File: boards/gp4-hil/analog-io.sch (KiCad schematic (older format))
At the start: 147 parts, among them U10 AD9609, U11 DAC084S085, U12 DAC084S085, U13 DAC084S085, U14 DAC084S085, U19 TS3A4751, U2 XC7A100T-1FTG256C, U25 TS3A4751, U26 TS3A4751, U27 TS3A4751, U28 TS3A4751, U31 ADA4937-2, U8 ADG726, U9 AD9609

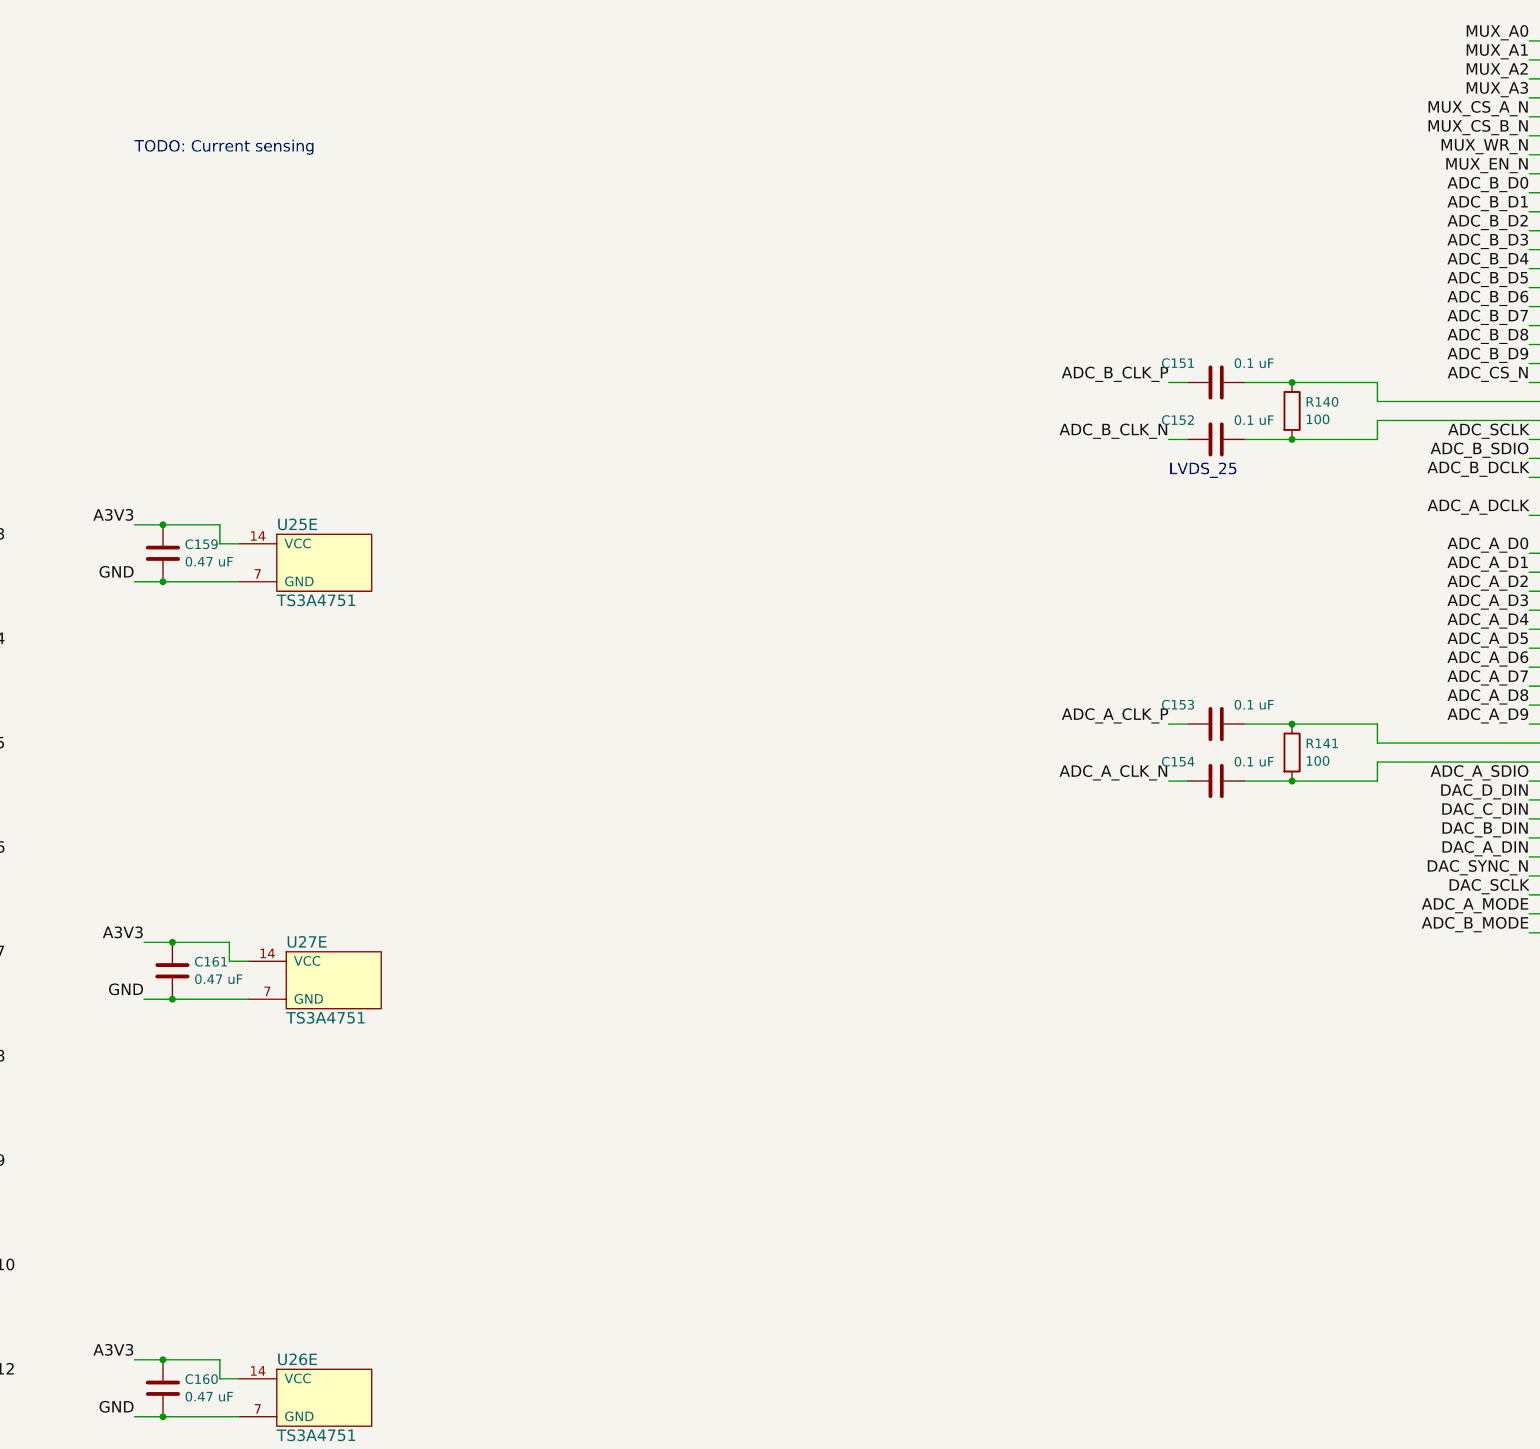
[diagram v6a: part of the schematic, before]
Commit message: Added current monitoring shunts. Began design review
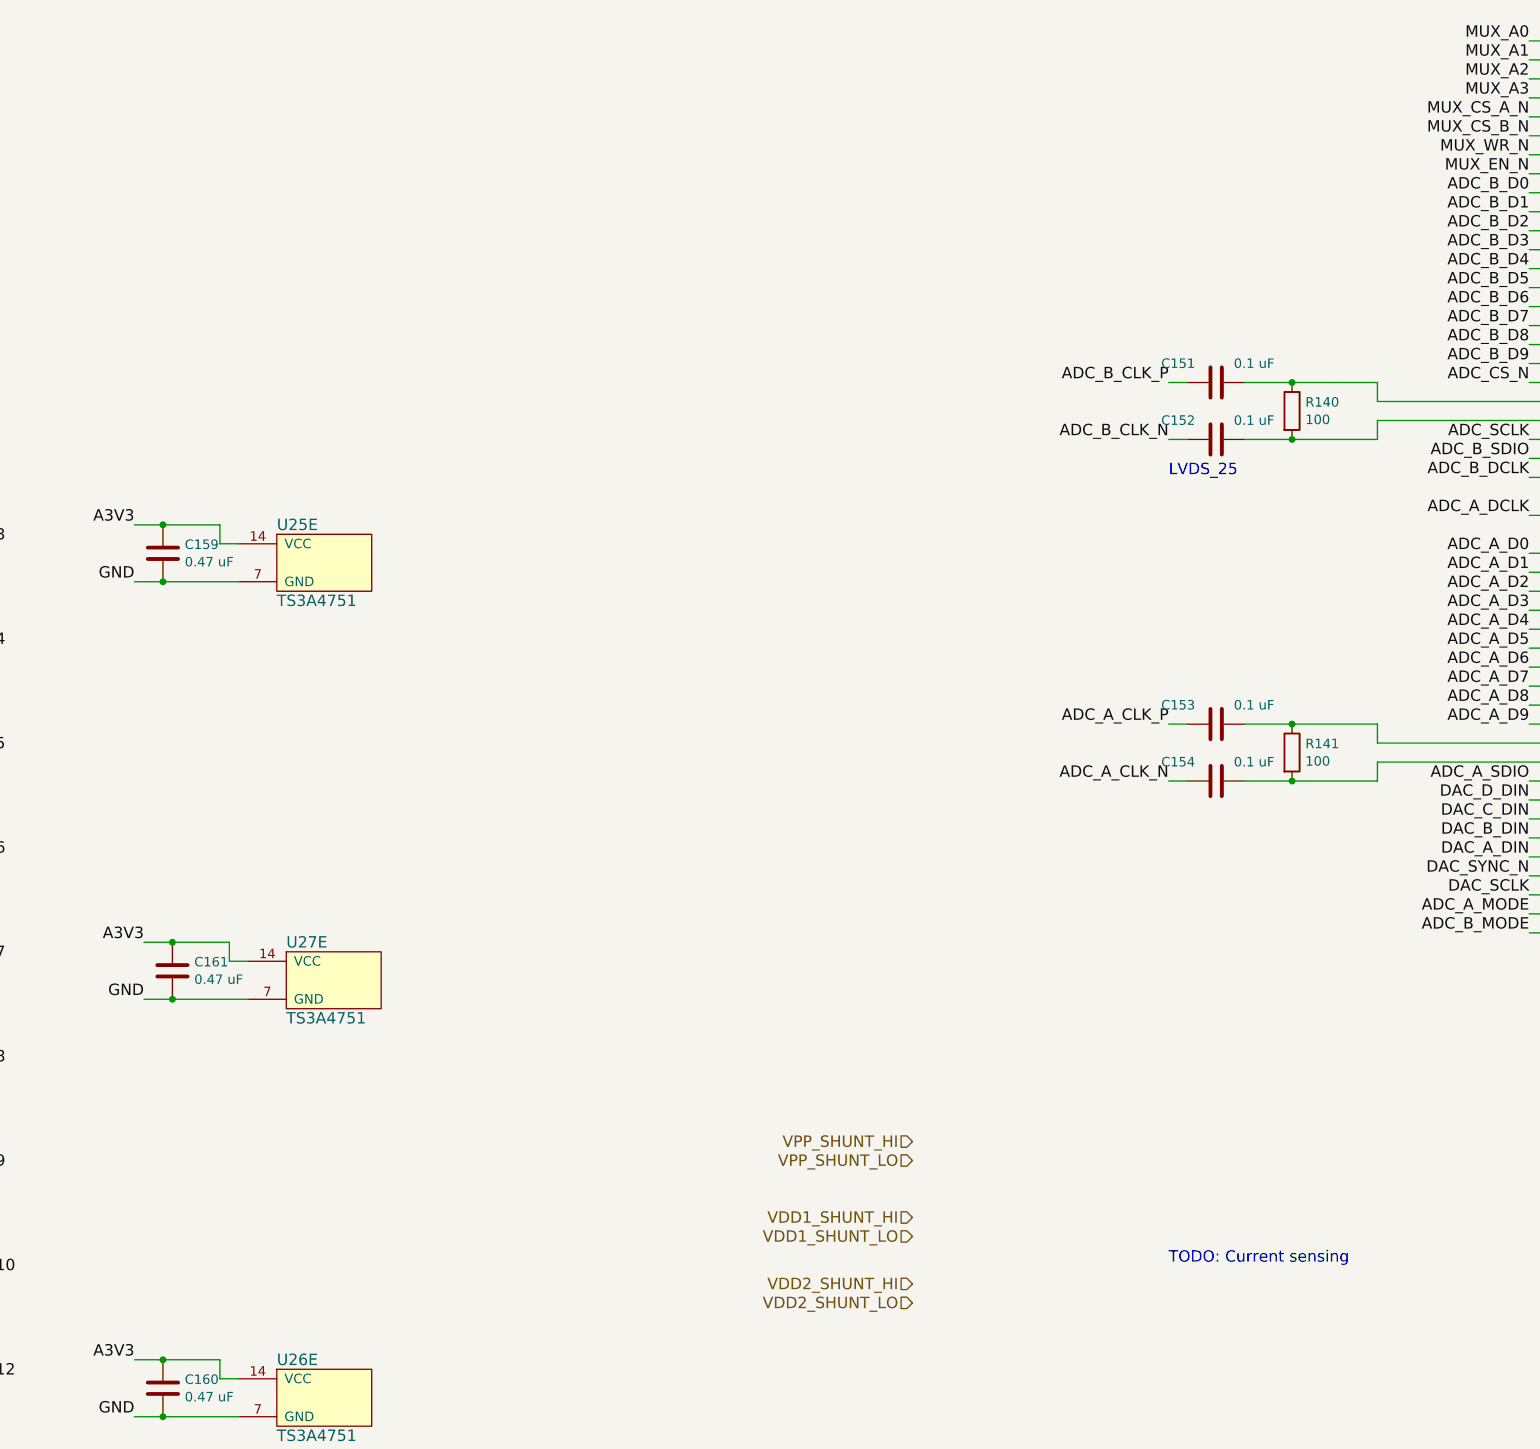
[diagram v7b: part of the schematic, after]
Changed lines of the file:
@@
 Sheet 5 7
 Title "GreenPak Hardware-In-Loop Test Platform"
-Date "2016-05-17"
+Date "2016-05-18"
 Rev "0.1"
 Comp "Andrew Zonenberg"
@@
 Text Label 20550 1850 2    60   ~ 0
 MUX_EN_N
-Text Notes 13200 1750 0    60   ~ 0
+Text Notes 18650 7600 0    60   ~ 0
 TODO: Current sensing
 $Comp
@@
 Wire Wire Line
 	1300 700  1500 700
+Text HLabel 17300 6950 0    60   Input ~ 0
+VPP_SHUNT_HI
+Text HLabel 17300 7050 0    60   Input ~ 0
+VPP_SHUNT_LO
+Text HLabel 17300 7350 0    60   Input ~ 0
+VDD1_SHUNT_HI
+Text HLabel 17300 7450 0    60   Input ~ 0
+VDD1_SHUNT_LO
+Text HLabel 17300 7700 0    60   Input ~ 0
+VDD2_SHUNT_HI
+Text HLabel 17300 7800 0    60   Input ~ 0
+VDD2_SHUNT_LO
 $EndSCHEMATC

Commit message: Added shunt amplifiers and connected to ADC
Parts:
- added C176, C177, C178: 0.1 uF, symbol C
- added U34, U35, U36: INA199A2RSW, symbol INA199AX-RSW
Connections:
- net A3V3: now also C176.1, C177.1, C178.1, U34.6 (VDD), U35.6 (VDD), U36.6 (VDD)
- net GND: now also C176.2, C177.2, C178.2, U34.8 (REF), U34.9 (GND), U35.8 (REF), U35.9 (GND), U36.8 (REF), U36.9 (GND)
- net VDD1_SHUNT_HI: now also U35.2 (IN+), U35.3 (IN+)
- net VDD1_SHUNT_LO: now also U35.4 (IN-), U35.5 (IN-)
- net VDD2_SHUNT_HI: now also U36.2 (IN+), U36.3 (IN+)
- net VDD2_SHUNT_LO: now also U36.4 (IN-), U36.5 (IN-)
- net VPP_SHUNT_HI: now also U34.2 (IN+), U34.3 (IN+)
- net VPP_SHUNT_LO: now also U34.4 (IN-), U34.5 (IN-)
- net VDD2_ISENSE: now reaches U8.36 (S12B)
- net VDD2_ISENSE: now also U36.10 (OUT)
- net VDD1_ISENSE: now reaches U8.4 (S13A)
- net VDD1_ISENSE: now also U35.10 (OUT)
- net VPP_ISENSE: now reaches U8.5 (S12A)
- net VPP_ISENSE: now also U34.10 (OUT)
- no-connect marks 17 -> 14
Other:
- note added: "DUT current metering"
- note removed: "TODO: Current sensing"
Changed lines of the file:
@@
 Sheet 5 7
 Title "GreenPak Hardware-In-Loop Test Platform"
-Date "2016-05-18"
+Date "2016-05-19"
 Rev "0.1"
 Comp "Andrew Zonenberg"
-Comment1 ""
+Comment1 "ADCs and DACs"
 Comment2 ""
 Comment3 ""
@@
 	1    0    0    -1
 $EndComp
-NoConn ~ 1650 6350
-NoConn ~ 1650 6450
 NoConn ~ 1650 6550
 NoConn ~ 1650 6650
 NoConn ~ 1650 6750
-NoConn ~ 3050 6350
 NoConn ~ 3050 6450
 NoConn ~ 3050 6550
@@
 Text Label 20550 1850 2    60   ~ 0
 MUX_EN_N
-Text Notes 18650 7600 0    60   ~ 0
-TODO: Current sensing
+Text Notes 17150 12250 0    60   ~ 0
+DUT current metering
 $Comp
 L AD9609 U9
@@
 	3050 6050 3150 6050
 Wire Wire Line
-	3150 6250 3050 6250
+	3050 6250 3450 6250
 Wire Wire Line
 	1700 7550 2950 7550
@@
 NoConn ~ 7650 7800
 NoConn ~ 7650 7600
-Text HLabel 3150 6250 2    60   Input ~ 0
+Text HLabel 3450 6250 2    60   Input ~ 0
 PSU_VTEMP
 Wire Wire Line
@@
 Wire Wire Line
 	1300 700  1500 700
-Text HLabel 17300 6950 0    60   Input ~ 0
+Text HLabel 17300 9350 0    60   Input ~ 0
 VPP_SHUNT_HI
-Text HLabel 17300 7050 0    60   Input ~ 0
+Text HLabel 17300 9450 0    60   Input ~ 0
 VPP_SHUNT_LO
-Text HLabel 17300 7350 0    60   Input ~ 0
+Text HLabel 17300 10550 0    60   Input ~ 0
 VDD1_SHUNT_HI
-Text HLabel 17300 7450 0    60   Input ~ 0
+Text HLabel 17300 10650 0    60   Input ~ 0
 VDD1_SHUNT_LO
-Text HLabel 17300 7700 0    60   Input ~ 0
+Text HLabel 17300 11700 0    60   Input ~ 0
 VDD2_SHUNT_HI
-Text HLabel 17300 7800 0    60   Input ~ 0
+Text HLabel 17300 11800 0    60   Input ~ 0
 VDD2_SHUNT_LO
+$Comp
+L INA199AX-RSW U34
+U 1 1 576C8568
+P 17750 9600
+F 0 "U34" H 17750 9550 60  0000 L CNN
+F 1 "INA199A2RSW" H 18550 9550 60  0000 R CNN
+F 2 "" H 17750 9600 60  0000 C CNN
+F 3 "" H 17750 9600 60  0000 C CNN
+	1    17750 9600
+	1    0    0    -1
+$EndComp
+Text Label 16750 8750 2    60   ~ 0
+A3V3
+Text Label 16750 9050 2    60   ~ 0
+GND
+Wire Wire Line
+	17300 9350 17450 9350
+Wire Wire Line
+	17450 9250 17350 9250
+Wire Wire Line
+	17350 9250 17350 9350
+Connection ~ 17350 9350
+Wire Wire Line
+	17300 9450 17450 9450
+Wire Wire Line
+	17450 9550 17350 9550
+Wire Wire Line
+	17350 9550 17350 9450
+Connection ~ 17350 9450
+Wire Wire Line
+	16750 9050 17450 9050
+$Comp
+L C C176
+U 1 1 576CB8B1
+P 16900 8900
+F 0 "C176" H 17015 8946 50  0000 L CNN
+F 1 "0.1 uF" H 17015 8854 50  0000 L CNN
+F 2 "" H 16938 8750 30  0000 C CNN
+F 3 "" H 16900 8900 60  0000 C CNN
+	1    16900 8900
+	1    0    0    -1
+$EndComp
+Connection ~ 16900 9050
+Wire Wire Line
+	16750 8750 17450 8750
+Connection ~ 16900 8750
+Wire Wire Line
+	17450 8750 17450 8850
+Wire Wire Line
+	17450 8950 17350 8950
+Wire Wire Line
+	17350 8950 17350 9050
+Connection ~ 17350 9050
+Text Label 19000 9400 0    60   ~ 0
+VPP_ISENSE
+Wire Wire Line
+	19000 9400 18800 9400
+$Comp
+L INA199AX-RSW U35
+U 1 1 576D207C
+P 17750 10800
+F 0 "U35" H 17750 10750 60  0000 L CNN
+F 1 "INA199A2RSW" H 18550 10750 60  0000 R CNN
+F 2 "" H 17750 10800 60  0000 C CNN
+F 3 "" H 17750 10800 60  0000 C CNN
+	1    17750 10800
+	1    0    0    -1
+$EndComp
+Text Label 16750 9950 2    60   ~ 0
+A3V3
+Text Label 16750 10250 2    60   ~ 0
+GND
+Wire Wire Line
+	17300 10550 17450 10550
+Wire Wire Line
+	17450 10450 17350 10450
+Wire Wire Line
+	17350 10450 17350 10550
+Connection ~ 17350 10550
+Wire Wire Line
+	17300 10650 17450 10650
+Wire Wire Line
+	17450 10750 17350 10750
+Wire Wire Line
+	17350 10750 17350 10650
+Connection ~ 17350 10650
+Wire Wire Line
+	16750 10250 17450 10250
+$Comp
+L C C177
+U 1 1 576D208D
+P 16900 10100
+F 0 "C177" H 17015 10146 50  0000 L CNN
+F 1 "0.1 uF" H 17015 10054 50  0000 L CNN
+F 2 "" H 16938 9950 30  0000 C CNN
+F 3 "" H 16900 10100 60  0000 C CNN
+	1    16900 10100
+	1    0    0    -1
+$EndComp
+Connection ~ 16900 10250
+Wire Wire Line
+	16750 9950 17450 9950
+Connection ~ 16900 9950
+Wire Wire Line
+	17450 9950 17450 10050
+Wire Wire Line
+	17450 10150 17350 10150
+Wire Wire Line
+	17350 10150 17350 10250
+Connection ~ 17350 10250
+Text Label 19000 10600 0    60   ~ 0
+VDD1_ISENSE
+Wire Wire Line
+	19000 10600 18800 10600
+$Comp
+L INA199AX-RSW U36
+U 1 1 576D2773
+P 17750 11950
+F 0 "U36" H 17750 11900 60  0000 L CNN
+F 1 "INA199A2RSW" H 18550 11900 60  0000 R CNN
+F 2 "" H 17750 11950 60  0000 C CNN
+F 3 "" H 17750 11950 60  0000 C CNN
+	1    17750 11950
+	1    0    0    -1
+$EndComp
+Text Label 16750 11100 2    60   ~ 0
+A3V3
+Text Label 16750 11400 2    60   ~ 0
+GND
+Wire Wire Line
+	17300 11700 17450 11700
+Wire Wire Line
+	17450 11600 17350 11600
+Wire Wire Line
+	17350 11600 17350 11700
+Connection ~ 17350 11700
+Wire Wire Line
+	17300 11800 17450 11800
+Wire Wire Line
+	17450 11900 17350 11900
+Wire Wire Line
+	17350 11900 17350 11800
+Connection ~ 17350 11800
+Wire Wire Line
+	16750 11400 17450 11400
+$Comp
+L C C178
+U 1 1 576D2784
+P 16900 11250
+F 0 "C178" H 17015 11296 50  0000 L CNN
+F 1 "0.1 uF" H 17015 11204 50  0000 L CNN
+F 2 "" H 16938 11100 30  0000 C CNN
+F 3 "" H 16900 11250 60  0000 C CNN
+	1    16900 11250
+	1    0    0    -1
+$EndComp
+Connection ~ 16900 11400
+Wire Wire Line
+	16750 11100 17450 11100
+Connection ~ 16900 11100
+Wire Wire Line
+	17450 11100 17450 11200
+Wire Wire Line
+	17450 11300 17350 11300
+Wire Wire Line
+	17350 11300 17350 11400
+Connection ~ 17350 11400
+Text Label 19000 11750 0    60   ~ 0
+VDD2_ISENSE
+Wire Wire Line
+	19000 11750 18800 11750
+Text Label 1550 6350 2    60   ~ 0
+VPP_ISENSE
+Text Label 1550 6450 2    60   ~ 0
+VDD1_ISENSE
+Text Label 3150 6350 0    60   ~ 0
+VDD2_ISENSE
+Wire Wire Line
+	3150 6350 3050 6350
+Wire Wire Line
+	1650 6450 1550 6450
+Wire Wire Line
+	1550 6350 1650 6350
 $EndSCHEMATC
